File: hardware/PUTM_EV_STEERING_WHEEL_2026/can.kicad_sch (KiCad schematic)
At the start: 10 parts, among them T13 TP_+3V3, T14 TP_+5V, T15 TP_CAN_H, T16 TP_CAN_L, U3 MCP2542FDxMF

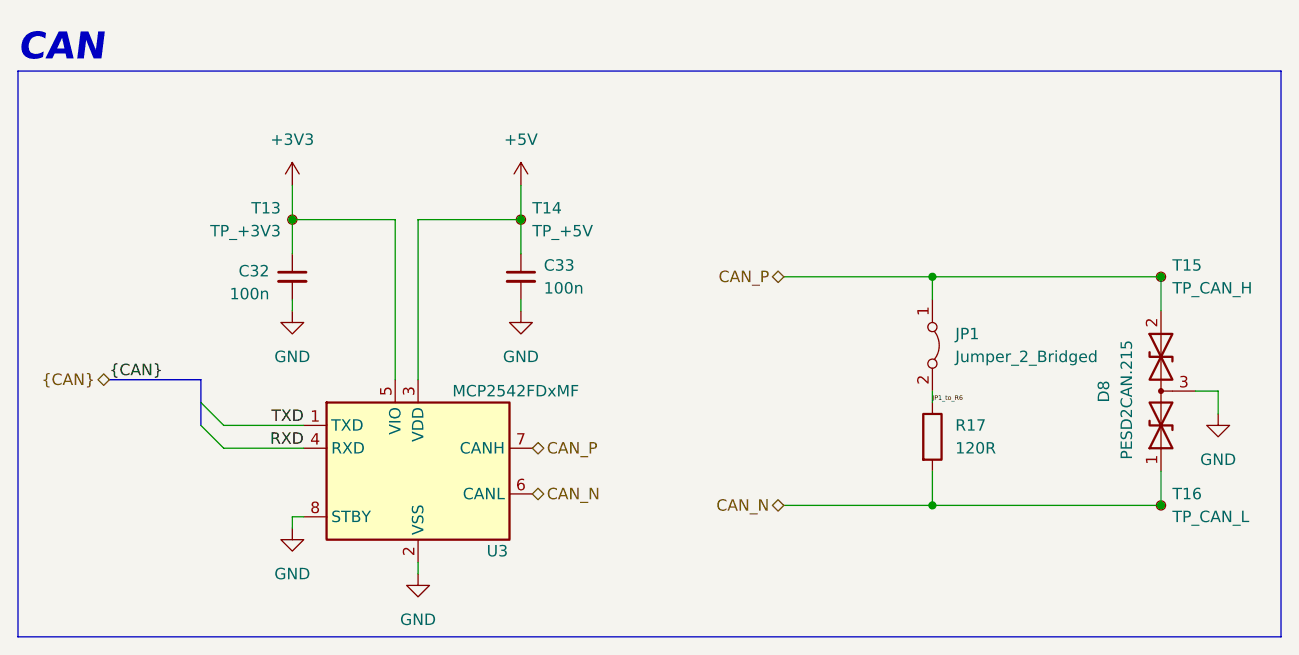
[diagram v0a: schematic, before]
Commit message: Edit MCU G0->G4, add RS in schema
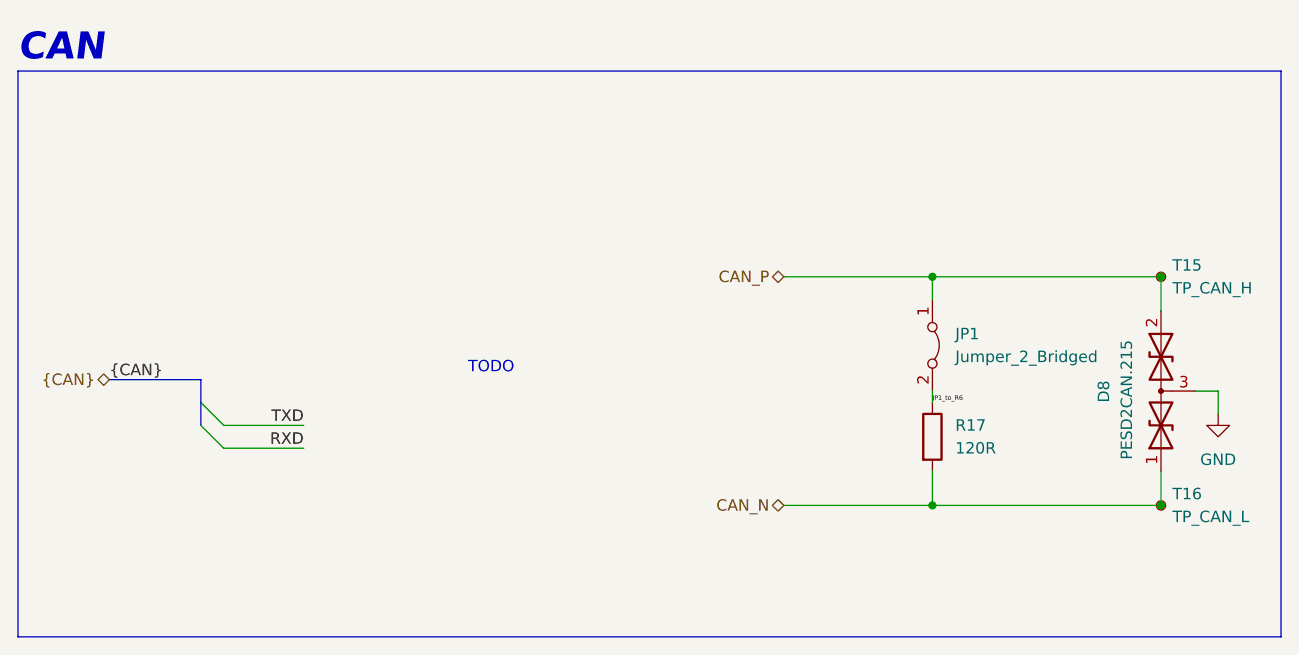
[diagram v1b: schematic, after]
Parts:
- removed C32, C33: 100n, Capacitor_SMD:C_0603_1608Metric_Pad1.08x0.95mm_HandSolder, symbol Device:C_Small
- removed T13: TP_+3V3, TestPoint:TestPoint_Pad_1.0x1.0mm, symbol Connector:TestPoint_Small
- removed T14: TP_+5V, TestPoint:TestPoint_Pad_1.0x1.0mm, symbol Connector:TestPoint_Small
- removed U3: MCP2542FDxMF, Package_DFN_QFN:DFN-8-1EP_3x3mm_P0.65mm_EP1.55x2.4mm, symbol Interface_CAN_LIN:MCP2542FDxMF
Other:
- note added: "TODO"
